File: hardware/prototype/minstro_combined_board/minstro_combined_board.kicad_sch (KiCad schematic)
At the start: 0 parts

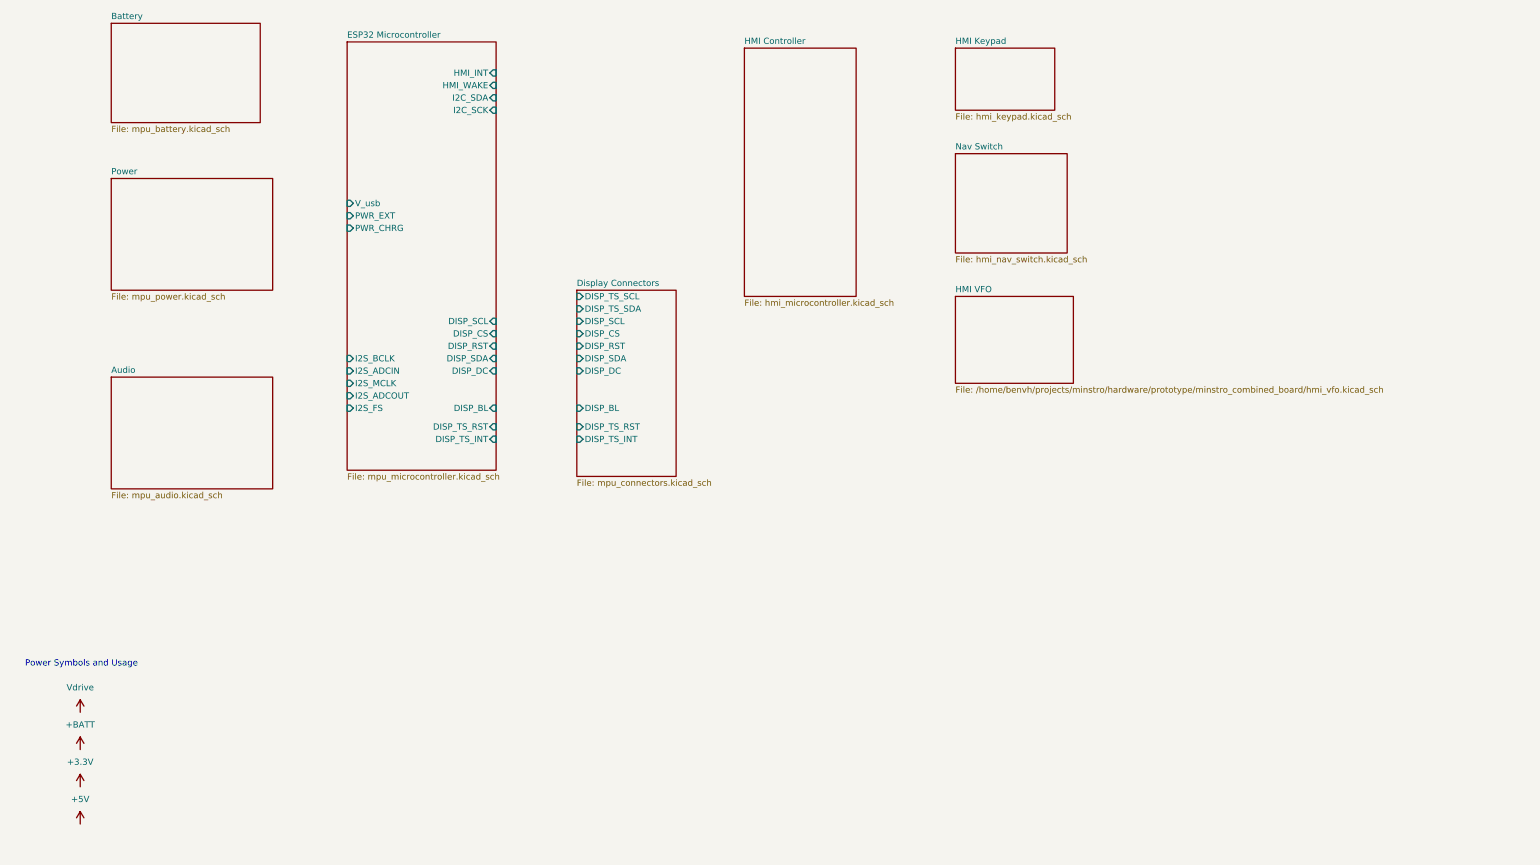
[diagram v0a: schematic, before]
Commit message: Schematic ERC complete
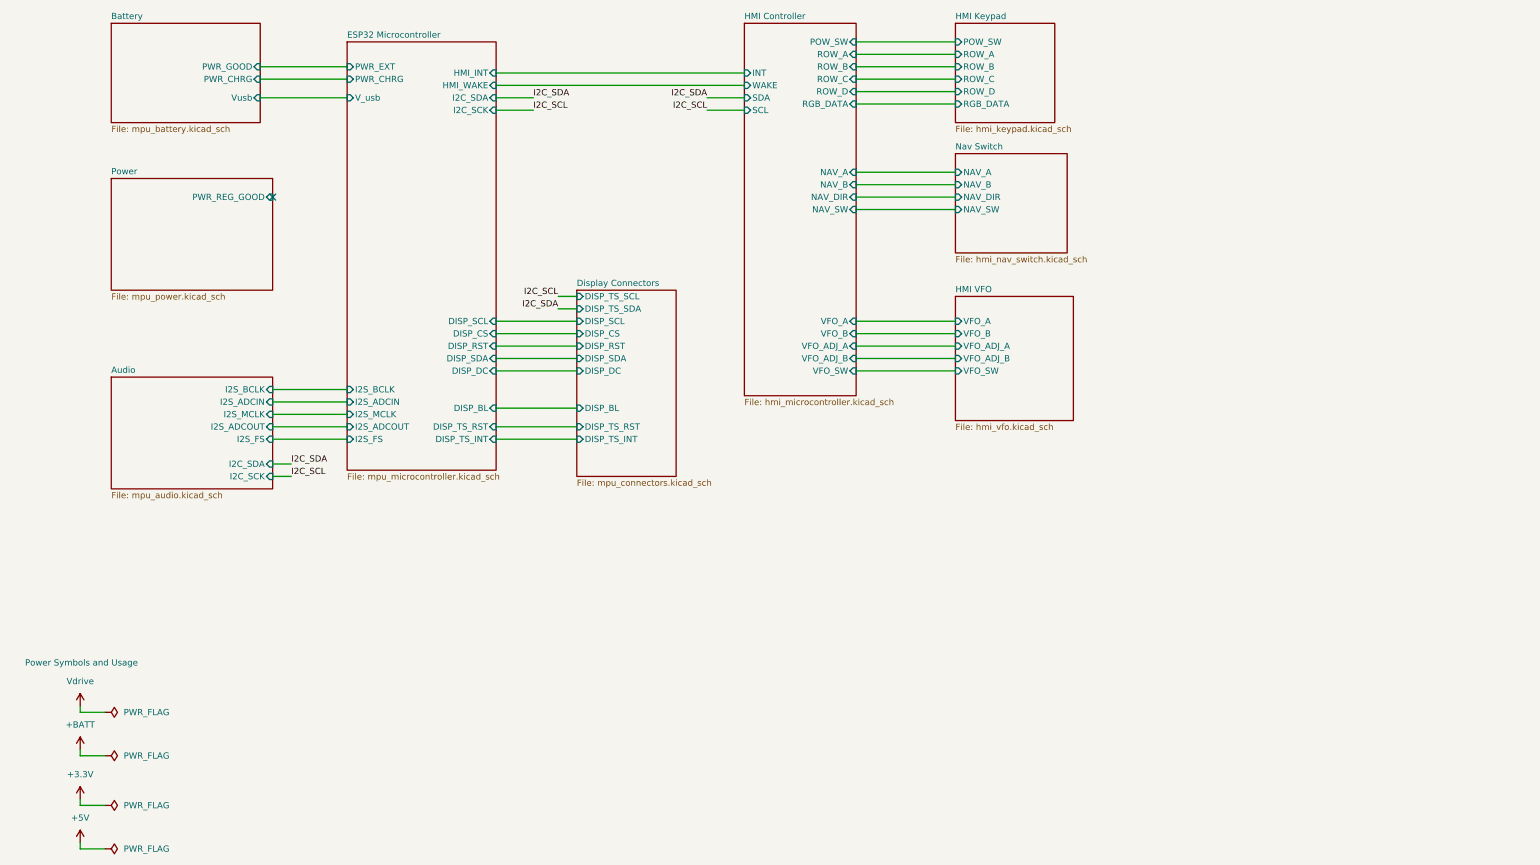
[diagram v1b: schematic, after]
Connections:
- no-connect marks 0 -> 1
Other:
- sheet Audio ports: added I2C_SCK, I2C_SDA, I2S_ADCIN, I2S_ADCOUT, I2S_BCLK, I2S_FS, I2S_MCLK; removed none
- sheet Battery ports: added PWR_CHRG, PWR_GOOD, Vusb; removed none
- sheet HMI Controller ports: added INT, NAV_A, NAV_B, NAV_DIR, NAV_SW, POW_SW, RGB_DATA, ROW_A, ROW_B, ROW_C, ROW_D, SCL, SDA, VFO_A, VFO_ADJ_A, VFO_ADJ_B, VFO_B, VFO_SW, WAKE; removed none
- sheet HMI Keypad ports: added POW_SW, RGB_DATA, ROW_A, ROW_B, ROW_C, ROW_D; removed none
- sheet HMI VFO: file /home/benvh/projects/minstro/hardware/prototype/minstro_combined_board/hmi_vfo.kicad_sch -> hmi_vfo.kicad_sch
- sheet HMI VFO ports: added VFO_A, VFO_ADJ_A, VFO_ADJ_B, VFO_B, VFO_SW; removed none
- sheet Nav Switch ports: added NAV_A, NAV_B, NAV_DIR, NAV_SW; removed none
- sheet Power ports: added PWR_REG_GOOD; removed none

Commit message: Layout WIP
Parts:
- added H101, H102, H103, H104: MountingHole_Pad_MP, MountingHole:MountingHole_3.2mm_M3_Pad, symbol Mechanical:MountingHole_Pad_MP
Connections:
- new net GND: H101.MP, H102.MP, H103.MP, H104.MP

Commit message: Routing mostly completed
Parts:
- H101, H102, H103, H104: symbol Mechanical:MountingHole_Pad_MP -> Mechanical:MountingHole_Pad
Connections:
- net GND: now also H101.1, H102.1, H103.1, H104.1; no longer H101.MP, H102.MP, H103.MP, H104.MP
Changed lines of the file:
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@@
 		)
+	)
+	(junction
+		(at 25.4 163.83)
+		(diameter 0)
+		(color 0 0 0 0)
 	)
 	(no_connect
@@
 	(wire
 		(pts
-			(xy 25.4 191.77) (xy 25.4 190.5)
-		)
-		(stroke
-			(width 0)
-			(type default)
-		)
-	)
-	(wire
-		(pts
 			(xy 110.49 107.95) (xy 127 107.95)
 		)
@@
 	(wire
 		(pts
+			(xy 17.78 163.83) (xy 25.4 163.83)
+		)
+		(stroke
+			(width 0)
+			(type default)
+		)
+	)
+	(wire
+		(pts
 			(xy 25.4 163.83) (xy 30.48 163.83)
 		)
@@
 	(wire
 		(pts
-			(xy 30.48 191.77) (xy 25.4 191.77)
-		)
-		(stroke
-			(width 0)
-			(type default)
-		)
-	)
-	(wire
-		(pts
 			(xy 25.4 172.72) (xy 30.48 172.72)
 		)
@@
 		(pts
 			(xy 153.67 40.64) (xy 161.29 40.64)
+		)
+		(stroke
+			(width 0)
+			(type default)
+		)
+	)
+	(wire
+		(pts
+			(xy 17.78 162.56) (xy 17.78 163.83)
 		)
 		(stroke
@@
 	(symbol
 		(lib_id "power:+5V")
-		(at 25.4 190.5 0)
+		(at 17.78 162.56 0)
+		(mirror y)
 		(unit 1)
 		(exclude_from_sim no)
@@
 		(on_board yes)
 		(dnp no)
-		(fields_autoplaced yes)
-		(property "Reference" "#PWR0104"
-			(at 25.4 194.31 0)
+		(property "Reference" "#PWR0109"
+			(at 17.78 166.37 0)
 			(effects
 				(font
@@
 		)
 		(property "Value" "+5V"
-			(at 25.4 185.42 0)
+			(at 17.78 157.48 0)
 			(effects
 				(font
@@
 		)
 		(property "Footprint" ""
-			(at 25.4 190.5 0)
+			(at 17.78 162.56 0)
 			(effects
 				(font
@@
 		)
 		(property "Datasheet" ""
-			(at 25.4 190.5 0)
+			(at 17.78 162.56 0)
 			(effects
 				(font
@@
 		)
 		(property "Description" "Power symbol creates a global label with name \"+5V\""
-			(at 25.4 190.5 0)
+			(at 17.78 162.56 0)
 			(effects
 				(font
@@
 			(project "minstro_combined_board"
 				(path "/edc2d64f-9cdb-4ab0-b2de-c3cfa55e1c10"
-					(reference "#PWR0104")
+					(reference "#PWR0109")
 					(unit 1)
 				)
@@
 	)
 	(symbol
-		(lib_id "Mechanical:MountingHole_Pad_MP")
+		(lib_id "Mechanical:MountingHole_Pad")
 		(at 237.49 125.73 0)
 		(unit 1)
@@
 			)
 		)
-		(property "Description" "Mounting Hole with connection as pad named MP"
+		(property "Description" "Mounting Hole with connection"
 			(at 237.49 125.73 0)
 			(effects
@@
 			)
 		)
-		(pin "MP"
+		(pin "1"
 		)
 		(instances
@@
 				(path "/edc2d64f-9cdb-4ab0-b2de-c3cfa55e1c10"
 					(reference "H104")
-					(unit 1)
-				)
-			)
-		)
-	)
-	(symbol
-		(lib_id "power:PWR_FLAG")
-		(at 30.48 191.77 270)
-		(unit 1)
-		(exclude_from_sim no)
-		(in_bom yes)
-		(on_board yes)
-		(dnp no)
-		(fields_autoplaced yes)
-		(property "Reference" "#FLG0104"
-			(at 32.385 191.77 0)
-			(effects
-				(font
-					(size 1.27 1.27)
-				)
-				(hide yes)
-			)
-		)
-		(property "Value" "PWR_FLAG"
-			(at 34.29 191.7699 90)
-			(effects
-				(font
-					(size 1.27 1.27)
-				)
-				(justify left)
-			)
-		)
-		(property "Footprint" ""
-			(at 30.48 191.77 0)
-			(effects
-				(font
-					(size 1.27 1.27)
-				)
-				(hide yes)
-			)
-		)
-		(property "Datasheet" "~"
-			(at 30.48 191.77 0)
-			(effects
-				(font
-					(size 1.27 1.27)
-				)
-				(hide yes)
-			)
-		)
-		(property "Description" "Special symbol for telling ERC where power comes from"
-			(at 30.48 191.77 0)
-			(effects
-				(font
-					(size 1.27 1.27)
-				)
-				(hide yes)
-			)
-		)
-		(pin "1"
-		)
-		(instances
-			(project "minstro_combined_board"
-				(path "/edc2d64f-9cdb-4ab0-b2de-c3cfa55e1c10"
-					(reference "#FLG0104")
 					(unit 1)
 				)
@@
 	)
 	(symbol
-		(lib_id "Mechanical:MountingHole_Pad_MP")
+		(lib_id "Mechanical:MountingHole_Pad")
 		(at 232.41 125.73 0)
 		(unit 1)
@@
 			)
 		)
-		(property "Description" "Mounting Hole with connection as pad named MP"
+		(property "Description" "Mounting Hole with connection"
 			(at 232.41 125.73 0)
 			(effects
@@
 			)
 		)
-		(pin "MP"
+		(pin "1"
 		)
 		(instances
@@
 	)
 	(symbol
-		(lib_id "Mechanical:MountingHole_Pad_MP")
+		(lib_id "Mechanical:MountingHole_Pad")
 		(at 227.33 125.73 0)
 		(unit 1)
@@
 			)
 		)
-		(property "Description" "Mounting Hole with connection as pad named MP"
+		(property "Description" "Mounting Hole with connection"
 			(at 227.33 125.73 0)
 			(effects
@@
 			)
 		)
-		(pin "MP"
+		(pin "1"
 		)
 		(instances
@@
 	)
 	(symbol
-		(lib_id "Mechanical:MountingHole_Pad_MP")
+		(lib_id "Mechanical:MountingHole_Pad")
 		(at 222.25 125.73 0)
 		(unit 1)
@@
 			)
 		)
-		(property "Description" "Mounting Hole with connection as pad named MP"
+		(property "Description" "Mounting Hole with connection"
 			(at 222.25 125.73 0)
 			(effects
@@
 			)
 		)
-		(pin "MP"
+		(pin "1"
 		)
 		(instances
